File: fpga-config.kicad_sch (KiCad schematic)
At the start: 31 parts, among them J1 PinHeader_2x7_P2mm_SMD_Shroud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, Q1 BSS138PW, Q2 BSS138PW, Q3 BSS138PW, SW1 CVS-03B, SW2 SW_KMR211NGLFS_SMD, U2 TPD4E05U06QDQARQ1, U3 S25FL128SAGNFI000, U4 XC7K160T-FFG676

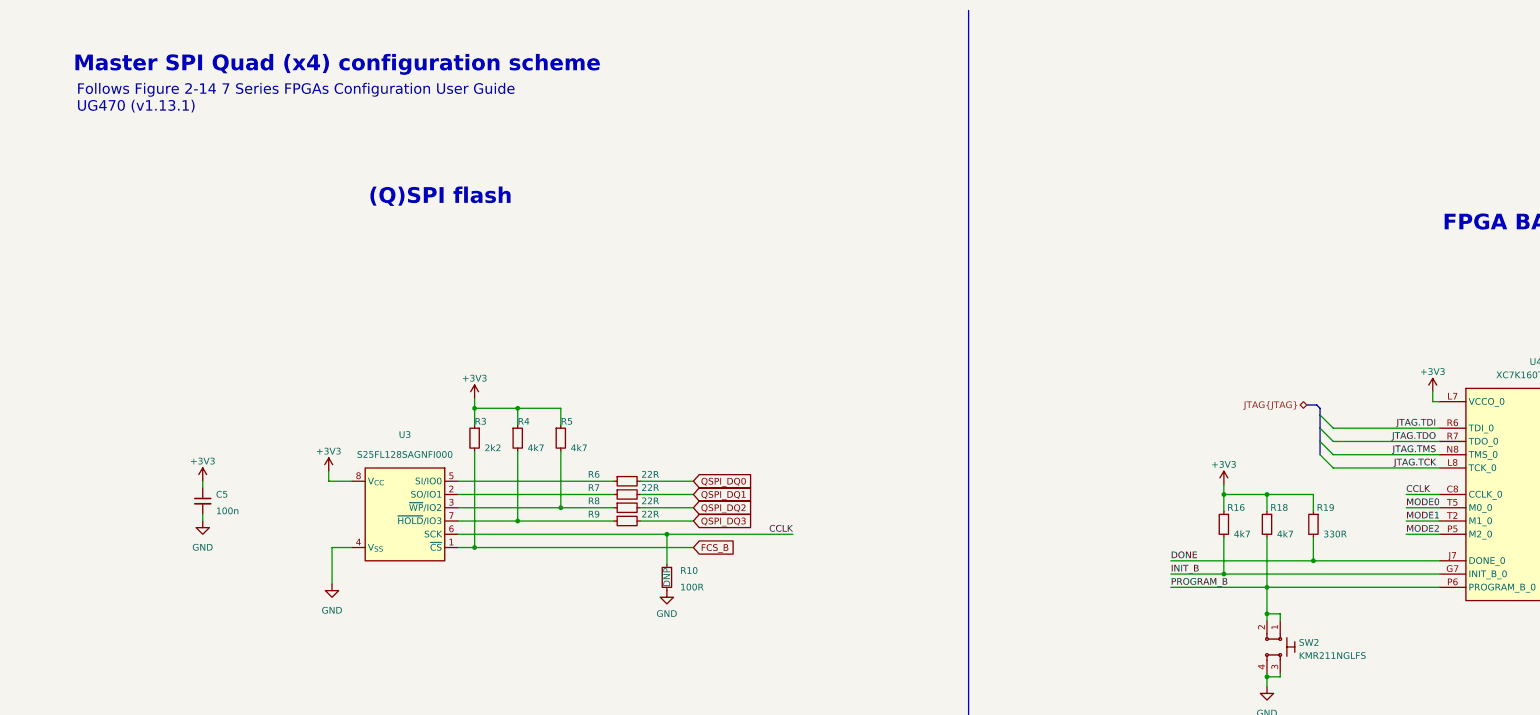
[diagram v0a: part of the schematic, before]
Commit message: Finish creating hierarchical buses and structure, start reconnecting signals
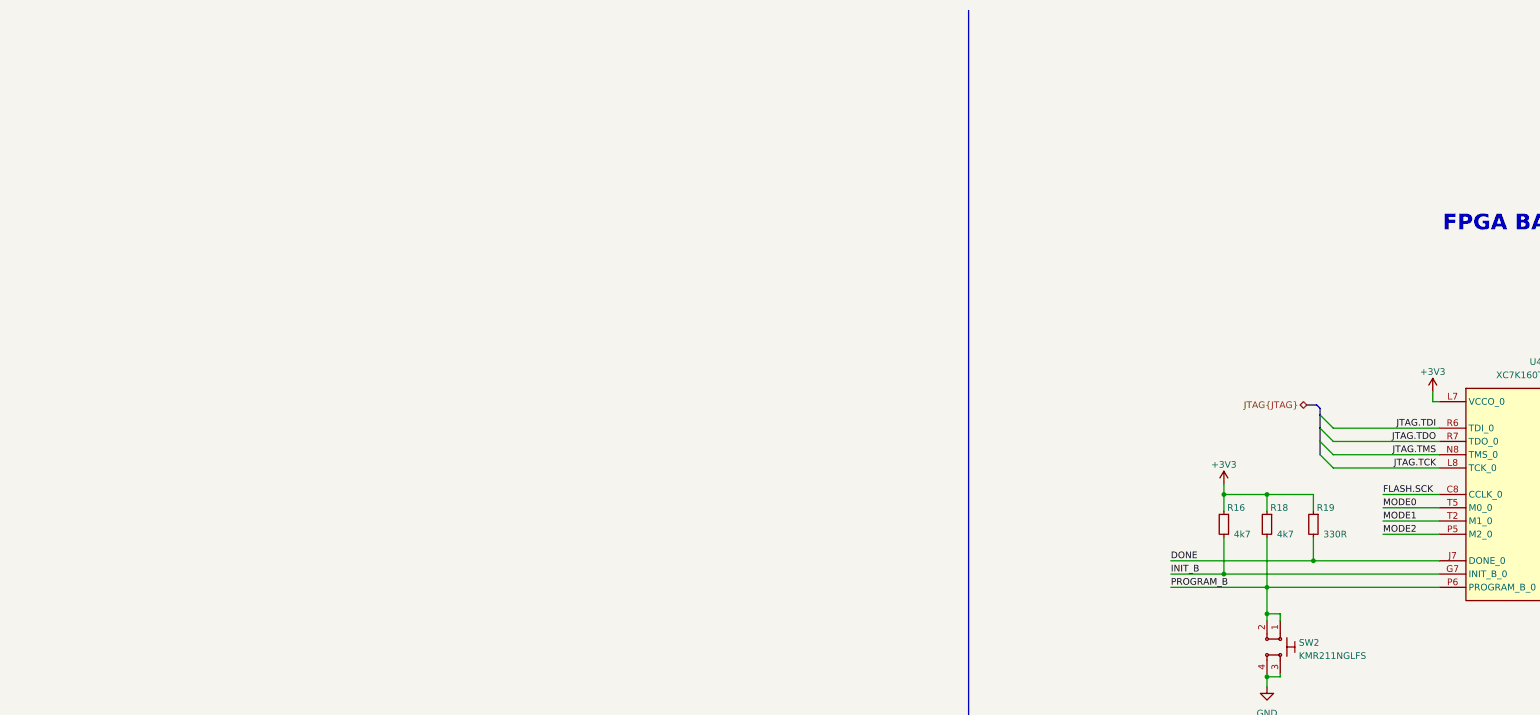
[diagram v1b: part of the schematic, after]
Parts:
- removed C5: C_100n_0402, sodimm-ddr5-tester-footprints:C_0402_1005Metric, symbol sodimm-ddr5-tester:C_100n_0402
- removed R10: R_100R_0402, sodimm-ddr5-tester-footprints:R_0402_1005Metric, symbol sodimm-ddr5-tester:R_100R_0402
- removed R3: R_2k2_0402, sodimm-ddr5-tester-footprints:R_0402_1005Metric, symbol sodimm-ddr5-tester:R_2k2_0402
- removed R4, R5: R_4k7_0402, sodimm-ddr5-tester-footprints:R_0402_1005Metric, symbol sodimm-ddr5-tester:R_4k7_0402
- removed R6, R7, R8, R9: R_22R_0402, sodimm-ddr5-tester-footprints:R_0402_1005Metric, symbol sodimm-ddr5-tester:R_22R_0402
- removed U3: S25FL128SAGNFI000, sodimm-ddr5-tester-footprints:WSON-8_6x8x0.5mm_P1.27mm, symbol sodimm-ddr5-tester:S25FL128SAGNFI000
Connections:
- net CCLK renamed FLASH.SCK
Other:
- note removed: "(Q)SPI flash"
- note removed: "Follows Figure 2-14 7 Series FPGAs Configuration User Guide UG470 (v1.13.1)"
- note removed: "Master SPI Quad (x4) configuration scheme"

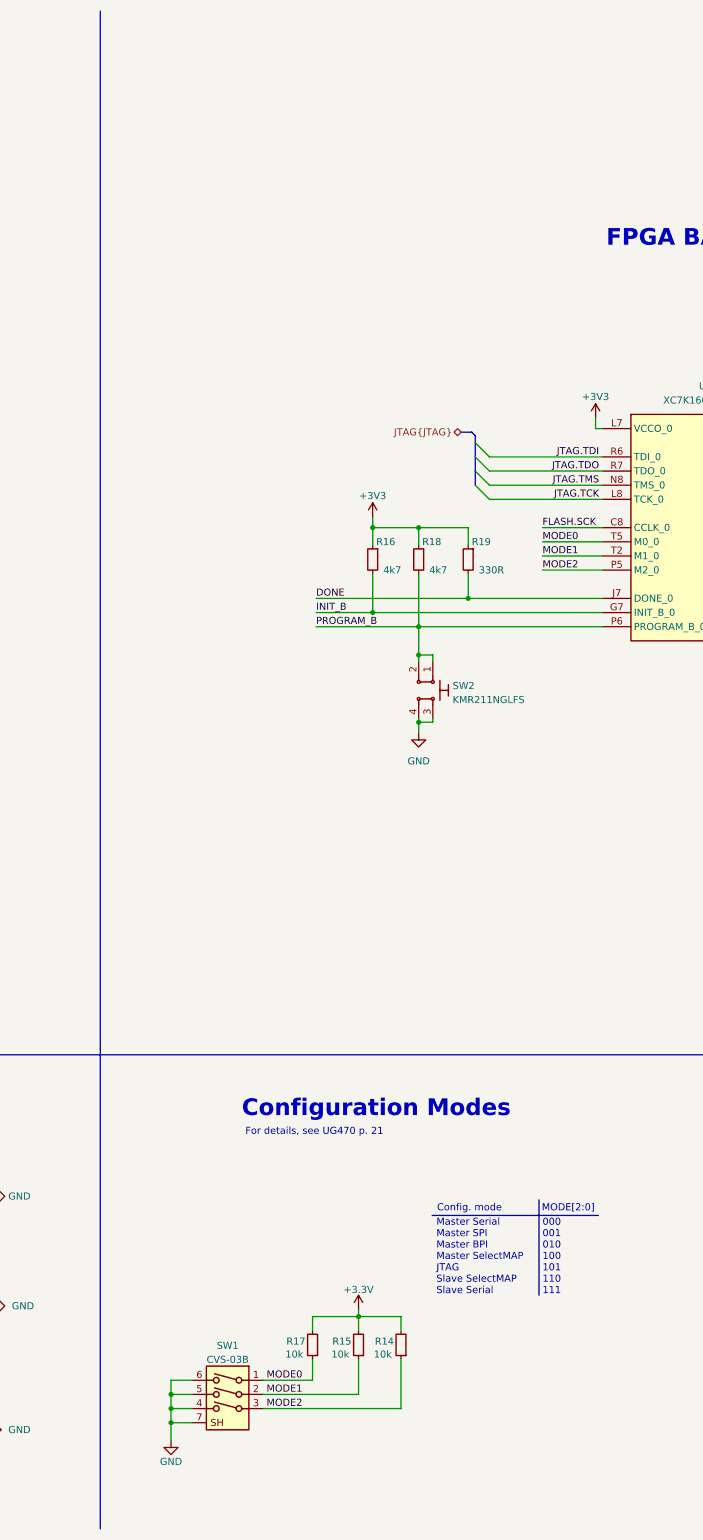
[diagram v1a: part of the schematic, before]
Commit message: Finish reconnecting signals after migration to the hierarchical structure
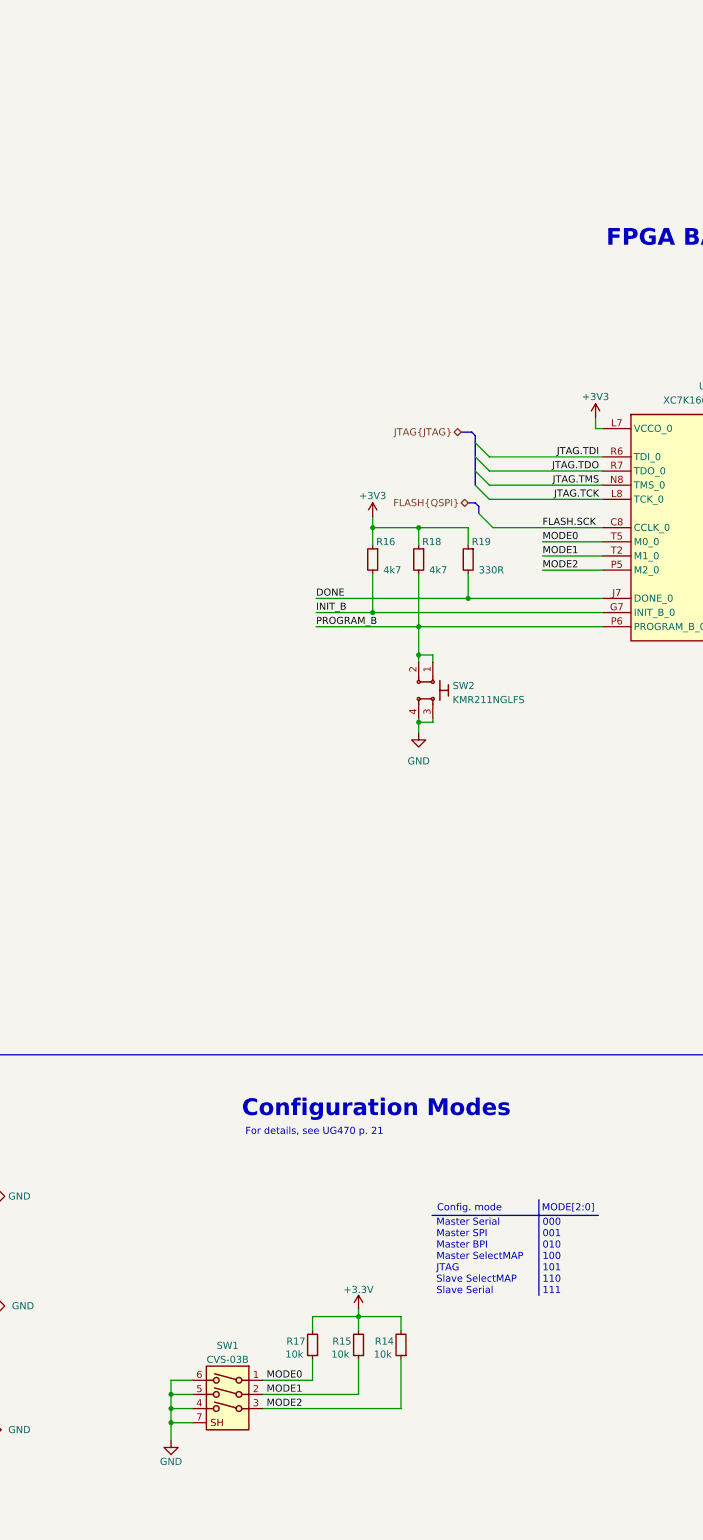
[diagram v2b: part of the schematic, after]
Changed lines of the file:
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@@
   (no_connect (at 42.545 242.57))
   (no_connect (at 42.545 240.03))
+  (bus_entry (at 266.065 105.41) (size -2.54 -2.54)
+    (stroke (width 0) (type default) (color 0 0 0 0))
+  )
   (bus_entry (at 265.43 97.79) (size -2.54 -2.54)
     (stroke (width 0) (type default) (color 0 0 0 0))
@@
     (stroke (width 0) (type default) (color 0 0 0 0))
   )
+  (bus (pts (xy 263.525 101.6) (xy 263.525 102.87))
+    (stroke (width 0) (type default) (color 0 0 0 0))
+  )
   (wire (pts (xy 241.935 247.015) (xy 241.935 249.555))
     (stroke (width 0) (type default) (color 0 0 0 0))
@@
     (stroke (width 0) (type default) (color 0 0 0 0))
   )
-  (wire (pts (xy 274.955 105.41) (xy 285.75 105.41))
+  (wire (pts (xy 266.065 105.41) (xy 285.75 105.41))
     (stroke (width 0) (type default) (color 0 0 0 0))
   )
@@
     (stroke (width 0) (type default) (color 0 0 0 0))
   )
+  (bus (pts (xy 261.62 100.965) (xy 262.89 100.965))
+    (stroke (width 0) (type default) (color 0 0 0 0))
+  )
   (wire (pts (xy 285.75 113.03) (xy 274.955 113.03))
     (stroke (width 0) (type default) (color 0 0 0 0))
@@
     (stroke (width 0) (type default) (color 0 0 0 0))
   )
+  (bus (pts (xy 262.89 100.965) (xy 263.525 101.6))
+    (stroke (width 0) (type default) (color 0 0 0 0))
+  )
   (wire (pts (xy 32.385 232.41) (xy 29.21 232.41))
     (stroke (width 0) (type default) (color 0 0 0 0))
@@
     (stroke (width 0) (type default) (color 0 0 0 0))
   )
-  (polyline (pts (xy 195.58 12.7) (xy 195.58 285.115))
-    (stroke (width 0) (type default) (color 0 0 0 0))
-  )
   (bus (pts (xy 262.89 90.17) (xy 262.89 92.71))
     (stroke (width 0) (type default) (color 0 0 0 0))
@@
     (effects (font (size 1.27 1.27)) (justify right))
     (property "Intersheet References" "${INTERSHEET_REFS}" (id 0) (at 129.6348 276.1456 0)
-      (effects (font (size 1.27 1.27)) (justify right) hide)
+      (effects (font (size 1.27 1.27)) (justify right))
     )
   )
@@
     (effects (font (size 1.27 1.27)) (justify right))
   )
+  (hierarchical_label "FLASH{QSPI}" (shape bidirectional) (at 261.62 100.965 180)
+    (effects (font (size 1.27 1.27)) (justify right))
+  )
   (symbol (lib_id "sodimm-ddr5-tester:GND") (at 29.21 247.015 0) (unit 1)
     (in_bom yes) (on_board yes) (fields_autoplaced)
-    (property "Reference" "#PWR?" (id 0) (at 29.21 253.365 0)
+    (property "Reference" "#PWR0182" (id 0) (at 29.21 253.365 0)
       (effects (font (size 1.27 1.27)) hide)
     )
@@
   (symbol (lib_id "sodimm-ddr5-tester:GND") (at 91.44 244.475 0) (unit 1)
     (in_bom yes) (on_board yes) (fields_autoplaced)
-    (property "Reference" "#PWR?" (id 0) (at 91.44 250.825 0)
+    (property "Reference" "#PWR0183" (id 0) (at 91.44 250.825 0)
       (effects (font (size 1.27 1.27)) hide)
     )
@@
   (symbol (lib_id "sodimm-ddr5-tester:GND") (at 175.895 225.425 90) (unit 1)
     (in_bom yes) (on_board yes) (fields_autoplaced)
-    (property "Reference" "#PWR?" (id 0) (at 182.245 225.425 0)
+    (property "Reference" "#PWR0186" (id 0) (at 182.245 225.425 0)
       (effects (font (size 1.27 1.27)) hide)
     )
@@
   (symbol (lib_id "sodimm-ddr5-tester:GND") (at 175.895 245.11 90) (unit 1)
     (in_bom yes) (on_board yes) (fields_autoplaced)
-    (property "Reference" "#PWR?" (id 0) (at 182.245 245.11 0)
+    (property "Reference" "#PWR0174" (id 0) (at 182.245 245.11 0)
       (effects (font (size 1.27 1.27)) hide)
     )
@@
   (symbol (lib_id "sodimm-ddr5-tester:GND") (at 252.73 142.24 0) (unit 1)
     (in_bom yes) (on_board yes) (fields_autoplaced)
-    (property "Reference" "#PWR?" (id 0) (at 252.73 148.59 0)
+    (property "Reference" "#PWR0187" (id 0) (at 252.73 148.59 0)
       (effects (font (size 1.27 1.27)) hide)
     )
@@
   (symbol (lib_id "sodimm-ddr5-tester:GND") (at 324.485 127.635 0) (mirror y) (unit 1)
     (in_bom yes) (on_board yes) (fields_autoplaced)
-    (property "Reference" "#PWR?" (id 0) (at 324.485 133.985 0)
+    (property "Reference" "#PWR0179" (id 0) (at 324.485 133.985 0)
       (effects (font (size 1.27 1.27)) hide)
     )
@@
   (symbol (lib_id "sodimm-ddr5-tester:+3V3") (at 284.48 85.725 0) (unit 1)
     (in_bom yes) (on_board yes)
-    (property "Reference" "#PWR?" (id 0) (at 284.48 89.535 0)
+    (property "Reference" "#PWR0180" (id 0) (at 284.48 89.535 0)
       (effects (font (size 1.27 1.27)) hide)
     )
@@
   (symbol (lib_id "sodimm-ddr5-tester:+3V3") (at 139.065 225.425 90) (unit 1)
     (in_bom yes) (on_board yes)
-    (property "Reference" "#PWR?" (id 0) (at 142.875 225.425 0)
+    (property "Reference" "#PWR0184" (id 0) (at 142.875 225.425 0)
       (effects (font (size 1.27 1.27)) hide)
     )
@@
   (symbol (lib_id "sodimm-ddr5-tester:+3V3") (at 47.625 222.885 0) (unit 1)
     (in_bom yes) (on_board yes)
-    (property "Reference" "#PWR?" (id 0) (at 47.625 226.695 0)
+    (property "Reference" "#PWR0185" (id 0) (at 47.625 226.695 0)
       (effects (font (size 1.27 1.27)) hide)
     )
@@
   (symbol (lib_id "sodimm-ddr5-tester:+3V3") (at 138.43 267.335 90) (unit 1)
     (in_bom yes) (on_board yes)
-    (property "Reference" "#PWR?" (id 0) (at 142.24 267.335 0)
+    (property "Reference" "#PWR0176" (id 0) (at 142.24 267.335 0)
       (effects (font (size 1.27 1.27)) hide)
     )
@@
   (symbol (lib_id "sodimm-ddr5-tester:+3V3") (at 244.475 103.505 0) (unit 1)
     (in_bom yes) (on_board yes)
-    (property "Reference" "#PWR?" (id 0) (at 244.475 107.315 0)
+    (property "Reference" "#PWR0188" (id 0) (at 244.475 107.315 0)
       (effects (font (size 1.27 1.27)) hide)
     )
@@
   (symbol (lib_id "sodimm-ddr5-tester:+3.3V") (at 241.935 245.745 0) (unit 1)
     (in_bom yes) (on_board yes) (fields_autoplaced)
-    (property "Reference" "#PWR?" (id 0) (at 241.935 249.555 0)
+    (property "Reference" "#PWR0189" (id 0) (at 241.935 249.555 0)
       (effects (font (size 1.27 1.27)) hide)
     )
@@
   (symbol (lib_id "sodimm-ddr5-tester:GND") (at 175.26 267.335 90) (unit 1)
     (in_bom yes) (on_board yes) (fields_autoplaced)
-    (property "Reference" "#PWR?" (id 0) (at 181.61 267.335 0)
+    (property "Reference" "#PWR0175" (id 0) (at 181.61 267.335 0)
       (effects (font (size 1.27 1.27)) hide)
     )
@@
   (symbol (lib_id "sodimm-ddr5-tester:+3V3") (at 329.565 85.09 0) (unit 1)
     (in_bom yes) (on_board yes)
-    (property "Reference" "#PWR?" (id 0) (at 329.565 88.9 0)
+    (property "Reference" "#PWR0181" (id 0) (at 329.565 88.9 0)
       (effects (font (size 1.27 1.27)) hide)
     )
@@
   (symbol (lib_id "sodimm-ddr5-tester:+3V3") (at 139.065 245.11 90) (unit 1)
     (in_bom yes) (on_board yes)
-    (property "Reference" "#PWR?" (id 0) (at 142.875 245.11 0)
+    (property "Reference" "#PWR0178" (id 0) (at 142.875 245.11 0)
       (effects (font (size 1.27 1.27)) hide)
     )
@@
   (symbol (lib_id "sodimm-ddr5-tester:GND") (at 208.28 269.24 0) (mirror y) (unit 1)
     (in_bom yes) (on_board yes)
-    (property "Reference" "#PWR?" (id 0) (at 208.28 275.59 0)
+    (property "Reference" "#PWR0177" (id 0) (at 208.28 275.59 0)
       (effects (font (size 1.27 1.27)) hide)
     )

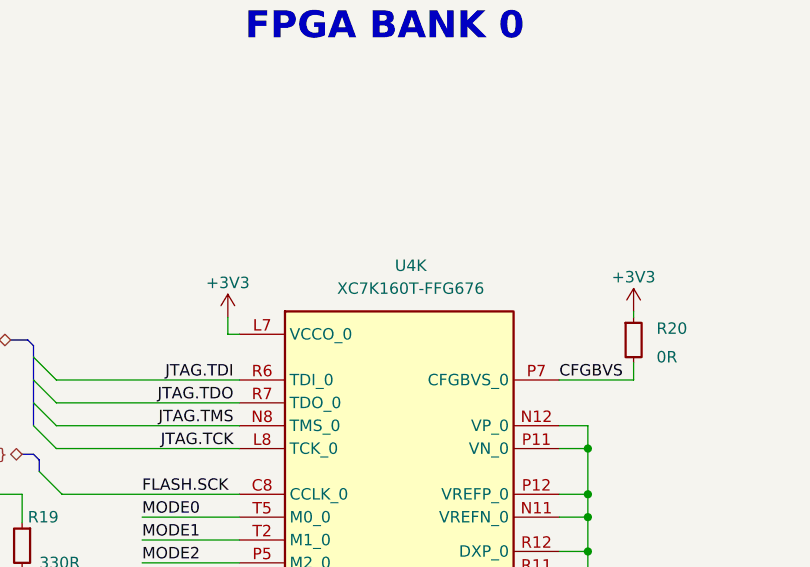
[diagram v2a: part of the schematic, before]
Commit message: Fix FPGA properties from the standardized library, update SO-DIMM symbol
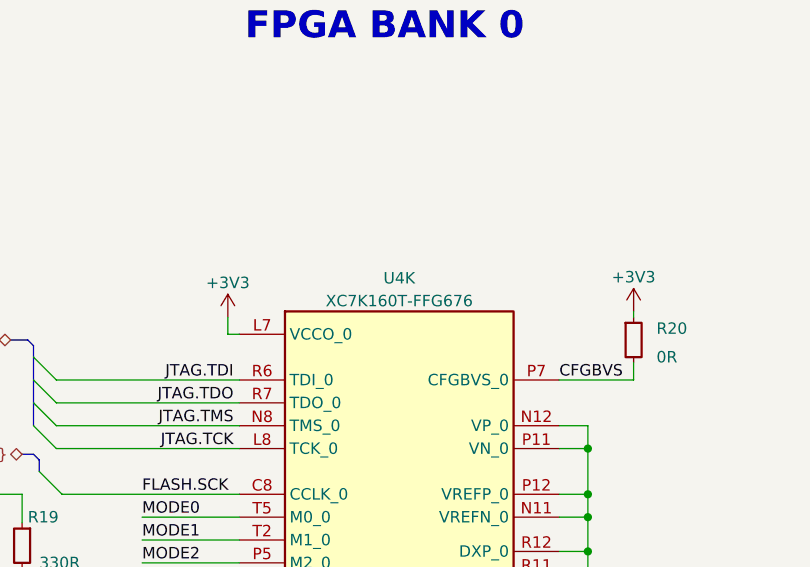
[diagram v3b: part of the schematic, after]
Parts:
- U4: footprint sodimm-ddr5-tester-footprints:BGA-676_27x27mm_Layout26x26_P1X1mm -> antmicro-footprints:BGA-676_27x27mm_Layout26x26_P1X1mm; symbol sodimm-ddr5-tester:XC7K160T-FFG676 -> antmicroMicrocontrollers:XC7K160T-FFG676; Manufacturer Xilinx -> AMD-Xilinx
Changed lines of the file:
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@@
     (pin "2")
   )
-  (symbol (lib_id "sodimm-ddr5-tester:XC7K160T-FFG676") (at 285.75 87.63 0) (unit 11)
+  (symbol (lib_id "antmicroMicrocontrollers:XC7K160T-FFG676") (at 285.75 87.63 0) (unit 11)
     (in_bom yes) (on_board yes) (fields_autoplaced)
-    (property "Reference" "U4" (id 0) (at 304.8 80.01 0))
-    (property "Value" "XC7K160T-FFG676" (id 1) (at 304.8 82.55 0)
+    (property "Reference" "U4" (id 0) (at 303.53 81.3984 0))
+    (property "Value" "XC7K160T-FFG676" (id 1) (at 303.53 83.9287 0)
       (effects (font (size 1.27 1.27) (thickness 0.15)))
     )
-    (property "Footprint" "sodimm-ddr5-tester-footprints:BGA-676_27x27mm_Layout26x26_P1X1mm" (id 2) (at 354.33 90.17 0)
+    (property "Footprint" "antmicro-footprints:BGA-676_27x27mm_Layout26x26_P1X1mm" (id 2) (at 354.33 90.17 0)
       (effects (font (size 1.27 1.27) (thickness 0.15)) (justify left bottom) hide)
     )
@@
       (effects (font (size 1.27 1.27) (thickness 0.15)) (justify left bottom) hide)
     )
-    (property "Manufacturer" "Xilinx" (id 7) (at 285.75 87.63 0)
+    (property "Manufacturer" "AMD-Xilinx" (id 7) (at 285.75 87.63 0)
       (effects (font (size 1.27 1.27)) hide)
     )

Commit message: Loclib of the project
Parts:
- U4: footprint antmicro-footprints:BGA-676_27x27mm_Layout26x26_P1X1mm -> sodimm-ddr5-tester-footprints:BGA-676_27x27mm_Layout26x26_P1X1mm; symbol antmicroMicrocontrollers:XC7K160T-FFG676 -> sodimm-ddr5-tester:XC7K160T-FFG676

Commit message: Finish schematic cleanup
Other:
- moved on the sheet: D1, D2, D3, Q1, Q2, Q3, R11, R12, R13, R14, R15, R16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
